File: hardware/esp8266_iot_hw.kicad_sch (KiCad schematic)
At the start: 0 parts

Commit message: ESP8266 KiCad Libs
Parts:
- added SW1: RESET, symbol Switch:SW_Push
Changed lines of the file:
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@@
     (company "Lucas Martin Treser")
+  )
+  (symbol (lib_id "Switch:SW_Push") (at 180.34 97.79 0) (unit 1)
+    (in_bom yes) (on_board yes) (dnp no) (fields_autoplaced)
+    (property "Reference" "SW1" (at 180.34 90.17 0)
+      (effects (font (size 1.27 1.27)))
+    )
+    (property "Value" "RESET" (at 180.34 92.71 0)
+      (effects (font (size 1.27 1.27)))
+    )
+    (property "Footprint" "" (at 180.34 92.71 0)
+      (effects (font (size 1.27 1.27)) hide)
+    )
+    (property "Datasheet" "~" (at 180.34 92.71 0)
+      (effects (font (size 1.27 1.27)) hide)
+    )
+    (pin "1")
+    (pin "2")
+    (instances
+      (project "esp8266_iot_hw"
+        (path "/ace0786b-d37d-4cab-bd65-f65737e95a89"
+          (reference "SW1") (unit 1)
+        )
+      )
+    )
+  )
+  (symbol (lib_id "power:GND") (at 144.78 105.41 0) (unit 1)
+    (in_bom yes) (on_board yes) (dnp no) (fields_autoplaced)
+    (property "Reference" "#PWR02" (at 144.78 111.76 0)
+      (effects (font (size 1.27 1.27)) hide)
+    )
+    (property "Value" "GND" (at 144.78 110.49 0)
+      (effects (font (size 1.27 1.27)))
+    )
+    (property "Footprint" "" (at 144.78 105.41 0)
+      (effects (font (size 1.27 1.27)) hide)
+    )
+    (property "Datasheet" "" (at 144.78 105.41 0)
+      (effects (font (size 1.27 1.27)) hide)
+    )
+    (pin "1")
+    (instances
+      (project "esp8266_iot_hw"
+        (path "/ace0786b-d37d-4cab-bd65-f65737e95a89"
+          (reference "#PWR02") (unit 1)
+        )
+      )
+    )
+  )
+  (symbol (lib_id "power:+5V") (at 152.4 76.2 0) (unit 1)
+    (in_bom yes) (on_board yes) (dnp no) (fields_autoplaced)
+    (property "Reference" "#PWR01" (at 152.4 80.01 0)
+      (effects (font (size 1.27 1.27)) hide)
+    )
+    (property "Value" "+5V" (at 152.4 71.12 0)
+      (effects (font (size 1.27 1.27)))
+    )
+    (property "Footprint" "" (at 152.4 76.2 0)
+      (effects (font (size 1.27 1.27)) hide)
+    )
+    (property "Datasheet" "" (at 152.4 76.2 0)
+      (effects (font (size 1.27 1.27)) hide)
+    )
+    (pin "1")
+    (instances
+      (project "esp8266_iot_hw"
+        (path "/ace0786b-d37d-4cab-bd65-f65737e95a89"
+          (reference "#PWR01") (unit 1)
+        )
+      )
+    )
   )
   (sheet_instances

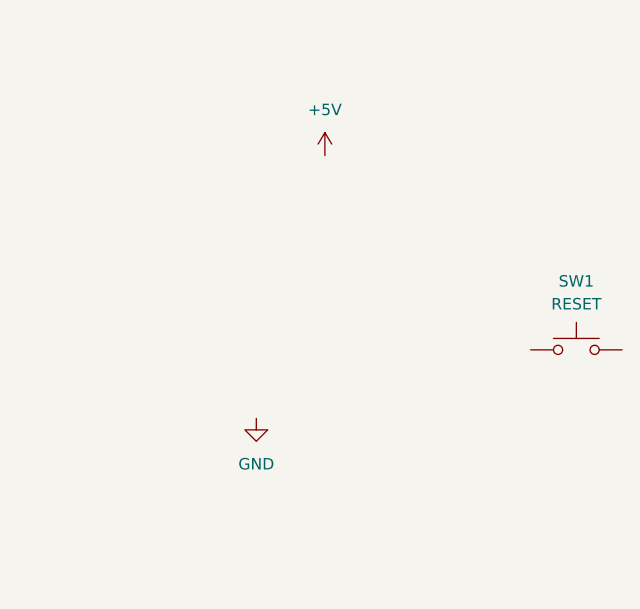
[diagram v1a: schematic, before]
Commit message: KiCad v7 schematics
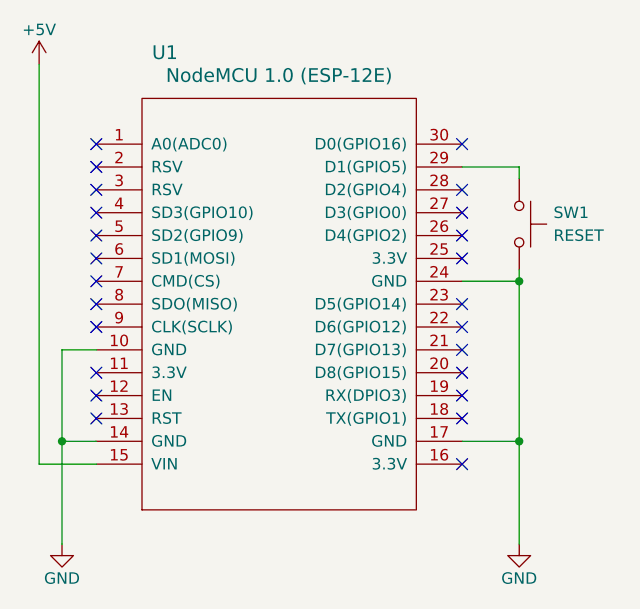
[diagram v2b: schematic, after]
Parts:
- added U1: NodeMCU 1.0 (ESP-12E), symbol ESP8266:NodeMCU1.0(ESP-12E)
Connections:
- net +5V: now also U1.15 (VIN)
- net GND: now also SW1.2, U1.10 (GND), U1.14 (GND), U1.17 (GND), U1.24 (GND)
- net at SW1.1: now also U1.29 (D1(GPIO5))
- no-connect marks 0 -> 24
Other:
- moved on the sheet: SW1
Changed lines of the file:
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@@
     (company "Lucas Martin Treser")
   )
-  (symbol (lib_id "Switch:SW_Push") (at 180.34 97.79 0) (unit 1)
+  (junction (at 123.19 107.95) (diameter 0) (color 0 0 0 0)
+  )
+  (junction (at 173.99 90.17) (diameter 0) (color 0 0 0 0)
+  )
+  (junction (at 173.99 107.95) (diameter 0) (color 0 0 0 0)
+  )
+  (no_connect (at 167.64 74.93))
+  (no_connect (at 167.64 82.55))
+  (no_connect (at 167.64 92.71))
+  (no_connect (at 127 95.25))
+  (no_connect (at 127 100.33))
+  (no_connect (at 167.64 100.33))
+  (no_connect (at 167.64 87.63))
+  (no_connect (at 127 82.55))
+  (no_connect (at 127 87.63))
+  (no_connect (at 127 92.71))
+  (no_connect (at 127 77.47))
+  (no_connect (at 167.64 85.09))
+  (no_connect (at 127 102.87))
+  (no_connect (at 167.64 80.01))
+  (no_connect (at 127 80.01))
+  (no_connect (at 127 85.09))
+  (no_connect (at 167.64 102.87))
+  (no_connect (at 167.64 110.49))
+  (no_connect (at 127 105.41))
+  (no_connect (at 127 90.17))
+  (no_connect (at 167.64 105.41))
+  (no_connect (at 127 74.93))
+  (no_connect (at 167.64 95.25))
+  (no_connect (at 167.64 97.79))
+  (wire (pts (xy 123.19 107.95) (xy 123.19 119.38))
+    (stroke (width 0) (type default))
+  )
+  (wire (pts (xy 120.65 110.49) (xy 127 110.49))
+    (stroke (width 0) (type default))
+  )
+  (wire (pts (xy 127 107.95) (xy 123.19 107.95))
+    (stroke (width 0) (type default))
+  )
+  (wire (pts (xy 167.64 107.95) (xy 173.99 107.95))
+    (stroke (width 0) (type default))
+  )
+  (wire (pts (xy 173.99 90.17) (xy 173.99 107.95))
+    (stroke (width 0) (type default))
+  )
+  (wire (pts (xy 127 97.79) (xy 123.19 97.79))
+    (stroke (width 0) (type default))
+  )
+  (wire (pts (xy 173.99 77.47) (xy 173.99 78.74))
+    (stroke (width 0) (type default))
+  )
+  (wire (pts (xy 123.19 97.79) (xy 123.19 107.95))
+    (stroke (width 0) (type default))
+  )
+  (wire (pts (xy 167.64 90.17) (xy 173.99 90.17))
+    (stroke (width 0) (type default))
+  )
+  (wire (pts (xy 167.64 77.47) (xy 173.99 77.47))
+    (stroke (width 0) (type default))
+  )
+  (wire (pts (xy 120.65 66.04) (xy 120.65 110.49))
+    (stroke (width 0) (type default))
+  )
+  (wire (pts (xy 173.99 90.17) (xy 173.99 88.9))
+    (stroke (width 0) (type default))
+  )
+  (wire (pts (xy 173.99 107.95) (xy 173.99 119.38))
+    (stroke (width 0) (type default))
+  )
+  (symbol (lib_id "power:GND") (at 173.99 119.38 0) (unit 1)
+    (in_bom yes) (on_board yes) (dnp no)
+    (property "Reference" "#PWR03" (at 173.99 125.73 0)
+      (effects (font (size 1.27 1.27)) hide)
+    )
+    (property "Value" "GND" (at 173.99 123.19 0)
+      (effects (font (size 1.27 1.27)))
+    )
+    (property "Footprint" "" (at 173.99 119.38 0)
+      (effects (font (size 1.27 1.27)) hide)
+    )
+    (property "Datasheet" "" (at 173.99 119.38 0)
+      (effects (font (size 1.27 1.27)) hide)
+    )
+    (pin "1")
+    (instances
+      (project "esp8266_iot_hw"
+        (path "/ace0786b-d37d-4cab-bd65-f65737e95a89"
+          (reference "#PWR03") (unit 1)
+        )
+      )
+    )
+  )
+  (symbol (lib_id "Switch:SW_Push") (at 173.99 83.82 270) (unit 1)
     (in_bom yes) (on_board yes) (dnp no) (fields_autoplaced)
-    (property "Reference" "SW1" (at 180.34 90.17 0)
+    (property "Reference" "SW1" (at 177.8 82.55 90)
+      (effects (font (size 1.27 1.27)) (justify left))
+    )
+    (property "Value" "RESET" (at 177.8 85.09 90)
+      (effects (font (size 1.27 1.27)) (justify left))
+    )
+    (property "Footprint" "" (at 179.07 83.82 0)
+      (effects (font (size 1.27 1.27)) hide)
+    )
+    (property "Datasheet" "~" (at 179.07 83.82 0)
+      (effects (font (size 1.27 1.27)) hide)
+    )
+    (pin "1")
+    (pin "2")
+    (instances
+      (project "esp8266_iot_hw"
+        (path "/ace0786b-d37d-4cab-bd65-f65737e95a89"
+          (reference "SW1") (unit 1)
+        )
+      )
+    )
+  )
+  (symbol (lib_id "power:GND") (at 123.19 119.38 0) (unit 1)
+    (in_bom yes) (on_board yes) (dnp no)
+    (property "Reference" "#PWR02" (at 123.19 125.73 0)
+      (effects (font (size 1.27 1.27)) hide)
+    )
+    (property "Value" "GND" (at 123.19 123.19 0)
       (effects (font (size 1.27 1.27)))
     )
-    (property "Value" "RESET" (at 180.34 92.71 0)
+    (property "Footprint" "" (at 123.19 119.38 0)
+      (effects (font (size 1.27 1.27)) hide)
+    )
+    (property "Datasheet" "" (at 123.19 119.38 0)
+      (effects (font (size 1.27 1.27)) hide)
+    )
+    (pin "1")
+    (instances
+      (project "esp8266_iot_hw"
+        (path "/ace0786b-d37d-4cab-bd65-f65737e95a89"
+          (reference "#PWR02") (unit 1)
+        )
+      )
+    )
+  )
+  (symbol (lib_id "power:+5V") (at 120.65 66.04 0) (unit 1)
+    (in_bom yes) (on_board yes) (dnp no)
+    (property "Reference" "#PWR01" (at 120.65 69.85 0)
+      (effects (font (size 1.27 1.27)) hide)
+    )
+    (property "Value" "+5V" (at 120.65 62.23 0)
       (effects (font (size 1.27 1.27)))
     )
-    (property "Footprint" "" (at 180.34 92.71 0)
-      (effects (font (size 1.27 1.27)) hide)
-    )
-    (property "Datasheet" "~" (at 180.34 92.71 0)
-      (effects (font (size 1.27 1.27)) hide)
-    )
-    (pin "1")
+    (property "Footprint" "" (at 120.65 66.04 0)
+      (effects (font (size 1.27 1.27)) hide)
+    )
+    (property "Datasheet" "" (at 120.65 66.04 0)
+      (effects (font (size 1.27 1.27)) hide)
+    )
+    (pin "1")
+    (instances
+      (project "esp8266_iot_hw"
+        (path "/ace0786b-d37d-4cab-bd65-f65737e95a89"
+          (reference "#PWR01") (unit 1)
+        )
+      )
+    )
+  )
+  (symbol (lib_id "ESP8266:NodeMCU1.0(ESP-12E)") (at 147.32 92.71 0) (unit 1)
+    (in_bom yes) (on_board yes) (dnp no)
+    (property "Reference" "U1" (at 134.62 64.77 0)
+      (effects (font (size 1.524 1.524)))
+    )
+    (property "Value" "NodeMCU 1.0 (ESP-12E)" (at 147.32 67.31 0)
+      (effects (font (size 1.524 1.524)))
+    )
+    (property "Footprint" "" (at 132.08 114.3 0)
+      (effects (font (size 1.524 1.524)))
+    )
+    (property "Datasheet" "" (at 132.08 114.3 0)
+      (effects (font (size 1.524 1.524)))
+    )
+    (pin "19")
+    (pin "7")
+    (pin "24")
+    (pin "11")
+    (pin "13")
+    (pin "27")
+    (pin "4")
+    (pin "25")
+    (pin "30")
+    (pin "1")
+    (pin "6")
+    (pin "5")
+    (pin "10")
+    (pin "21")
+    (pin "16")
+    (pin "18")
+    (pin "20")
+    (pin "3")
+    (pin "28")
+    (pin "26")
+    (pin "22")
+    (pin "29")
+    (pin "23")
+    (pin "9")
+    (pin "15")
+    (pin "14")
+    (pin "8")
     (pin "2")
-    (instances
-      (project "esp8266_iot_hw"
-        (path "/ace0786b-d37d-4cab-bd65-f65737e95a89"
-          (reference "SW1") (unit 1)
-        )
-      )
-    )
-  )
-  (symbol (lib_id "power:GND") (at 144.78 105.41 0) (unit 1)
-    (in_bom yes) (on_board yes) (dnp no) (fields_autoplaced)
-    (property "Reference" "#PWR02" (at 144.78 111.76 0)
-      (effects (font (size 1.27 1.27)) hide)
-    )
-    (property "Value" "GND" (at 144.78 110.49 0)
-      (effects (font (size 1.27 1.27)))
-    )
-    (property "Footprint" "" (at 144.78 105.41 0)
-      (effects (font (size 1.27 1.27)) hide)
-    )
-    (property "Datasheet" "" (at 144.78 105.41 0)
-      (effects (font (size 1.27 1.27)) hide)
-    )
-    (pin "1")
-    (instances
-      (project "esp8266_iot_hw"
-        (path "/ace0786b-d37d-4cab-bd65-f65737e95a89"
-          (reference "#PWR02") (unit 1)
-        )
-      )
-    )
-  )
-  (symbol (lib_id "power:+5V") (at 152.4 76.2 0) (unit 1)
-    (in_bom yes) (on_board yes) (dnp no) (fields_autoplaced)
-    (property "Reference" "#PWR01" (at 152.4 80.01 0)
-      (effects (font (size 1.27 1.27)) hide)
-    )
-    (property "Value" "+5V" (at 152.4 71.12 0)
-      (effects (font (size 1.27 1.27)))
-    )
-    (property "Footprint" "" (at 152.4 76.2 0)
-      (effects (font (size 1.27 1.27)) hide)
-    )
-    (property "Datasheet" "" (at 152.4 76.2 0)
-      (effects (font (size 1.27 1.27)) hide)
-    )
-    (pin "1")
-    (instances
-      (project "esp8266_iot_hw"
-        (path "/ace0786b-d37d-4cab-bd65-f65737e95a89"
-          (reference "#PWR01") (unit 1)
-        )
-      )
+    (pin "12")
+    (pin "17")
+    (instances
+      (project "esp8266_iot_hw"
+        (path "/ace0786b-d37d-4cab-bd65-f65737e95a89"
+          (reference "U1") (unit 1)
+        )
+      )

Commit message: add esp32 support
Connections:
- net at SW1.1: now also U1.28 (D2(GPIO4)); no longer U1.29 (D1(GPIO5))
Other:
- moved on the sheet: SW1
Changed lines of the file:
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@@
   (junction (at 123.19 107.95) (diameter 0) (color 0 0 0 0)
   )
-  (junction (at 173.99 90.17) (diameter 0) (color 0 0 0 0)
+  (junction (at 184.15 107.95) (diameter 0) (color 0 0 0 0)
   )
-  (junction (at 173.99 107.95) (diameter 0) (color 0 0 0 0)
+  (junction (at 184.15 90.17) (diameter 0) (color 0 0 0 0)
   )
   (no_connect (at 167.64 74.93))
   (no_connect (at 167.64 82.55))
+  (no_connect (at 167.64 77.47))
   (no_connect (at 167.64 92.71))
   (no_connect (at 127 95.25))
@@
   (no_connect (at 167.64 85.09))
   (no_connect (at 127 102.87))
-  (no_connect (at 167.64 80.01))
   (no_connect (at 127 80.01))
   (no_connect (at 127 85.09))
@@
     (stroke (width 0) (type default))
   )
-  (wire (pts (xy 167.64 107.95) (xy 173.99 107.95))
+  (wire (pts (xy 184.15 90.17) (xy 184.15 107.95))
     (stroke (width 0) (type default))
   )
-  (wire (pts (xy 173.99 90.17) (xy 173.99 107.95))
+  (wire (pts (xy 184.15 80.01) (xy 184.15 90.17))
     (stroke (width 0) (type default))
   )
@@
     (stroke (width 0) (type default))
   )
-  (wire (pts (xy 173.99 77.47) (xy 173.99 78.74))
-    (stroke (width 0) (type default))
-  )
   (wire (pts (xy 123.19 97.79) (xy 123.19 107.95))
     (stroke (width 0) (type default))
   )
-  (wire (pts (xy 167.64 90.17) (xy 173.99 90.17))
+  (wire (pts (xy 167.64 107.95) (xy 184.15 107.95))
     (stroke (width 0) (type default))
   )
-  (wire (pts (xy 167.64 77.47) (xy 173.99 77.47))
+  (wire (pts (xy 167.64 90.17) (xy 184.15 90.17))
+    (stroke (width 0) (type default))
+  )
+  (wire (pts (xy 181.61 80.01) (xy 184.15 80.01))
     (stroke (width 0) (type default))
   )
@@
     (stroke (width 0) (type default))
   )
-  (wire (pts (xy 173.99 90.17) (xy 173.99 88.9))
+  (wire (pts (xy 167.64 80.01) (xy 171.45 80.01))
     (stroke (width 0) (type default))
   )
-  (wire (pts (xy 173.99 107.95) (xy 173.99 119.38))
+  (wire (pts (xy 184.15 107.95) (xy 184.15 119.38))
     (stroke (width 0) (type default))
   )
-  (symbol (lib_id "power:GND") (at 173.99 119.38 0) (unit 1)
+  (symbol (lib_id "power:GND") (at 184.15 119.38 0) (unit 1)
     (in_bom yes) (on_board yes) (dnp no)
-    (property "Reference" "#PWR03" (at 173.99 125.73 0)
+    (property "Reference" "#PWR03" (at 184.15 125.73 0)
       (effects (font (size 1.27 1.27)) hide)
     )
-    (property "Value" "GND" (at 173.99 123.19 0)
+    (property "Value" "GND" (at 184.15 123.19 0)
       (effects (font (size 1.27 1.27)))
     )
-    (property "Footprint" "" (at 173.99 119.38 0)
+    (property "Footprint" "" (at 184.15 119.38 0)
       (effects (font (size 1.27 1.27)) hide)
     )
-    (property "Datasheet" "" (at 173.99 119.38 0)
+    (property "Datasheet" "" (at 184.15 119.38 0)
       (effects (font (size 1.27 1.27)) hide)
     )
@@
     )
   )
-  (symbol (lib_id "Switch:SW_Push") (at 173.99 83.82 270) (unit 1)
+  (symbol (lib_id "Switch:SW_Push") (at 176.53 80.01 0) (unit 1)
     (in_bom yes) (on_board yes) (dnp no) (fields_autoplaced)
-    (property "Reference" "SW1" (at 177.8 82.55 90)
-      (effects (font (size 1.27 1.27)) (justify left))
+    (property "Reference" "SW1" (at 176.53 72.39 0)
+      (effects (font (size 1.27 1.27)))
     )
-    (property "Value" "RESET" (at 177.8 85.09 90)
-      (effects (font (size 1.27 1.27)) (justify left))
+    (property "Value" "RESET" (at 176.53 74.93 0)
+      (effects (font (size 1.27 1.27)))
     )
-    (property "Footprint" "" (at 179.07 83.82 0)
+    (property "Footprint" "" (at 176.53 74.93 0)
       (effects (font (size 1.27 1.27)) hide)
     )
-    (property "Datasheet" "~" (at 179.07 83.82 0)
+    (property "Datasheet" "~" (at 176.53 74.93 0)
       (effects (font (size 1.27 1.27)) hide)
     )

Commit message: update schematics
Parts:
- added SW2: RESET, symbol Switch:SW_Push
- added U2: ESP32-DevKitC, PCM_Espressif:ESP32-DevKitC, symbol PCM_Espressif:ESP32-DevKitC
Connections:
- net +5V: now also U2.19 (5V)
- net GND: now also SW2.2, U2.14 (GND), U2.32 (GND), U2.38 (GND)
- new net: SW2.1, U2.26 (ADC2_CH0/GPIO4)
- no-connect marks 24 -> 56
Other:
- note added: "Versión ESP32"
- note added: "Versión ESP8266"
- title: DISPOSITIVO IOT GENERICO ESP8266 -> DISPOSITIVO IOT GENERICO ESP8266 & ESP32
- moved on the sheet: SW1, U1
